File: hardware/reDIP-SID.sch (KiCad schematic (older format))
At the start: 57 parts, among them J1 Conn_01x04, J2 Conn_01x04, J3 Conn_01x10, J4 Conn_01x10, J5 TYPE-C-31-M-12, J6 Conn_02x05_Odd_Even, Q1 PDTA143ZMB, SW1 KXT331LHS, U1 NCP163AMX120TBG, U2 NCP167AMX330TBG, U3 SN74CBTD16211DGVR, U4 SGTL5000XNLA3, U5 NUF2042XV6, U6 APS6404L-3SQR-SN, U7 W25Q128JVPIM, U8 ICE40UP5K-SG48I, X1 ASCO-24.576MHZ-EK-T

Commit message: Usability and manufacturability improvements
* Made all iCE40 RGB pins externally available
* Removed split in stencil apertures for pin-in-paste
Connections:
- net labels added: USB_~CONN~
- net labels removed: USB_CONN
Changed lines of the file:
@@
 Text Label 1000 5900 2    50   ~ 0
 USB_D+
+Text Label 1000 7400 2    50   ~ 0
+ICE_~IO1~
 Text Label 1000 7100 2    50   ~ 0
-ICE_~IO1~
-Text Label 1000 7400 2    50   ~ 0
-USB_CONN
+USB_~CONN~
 $Comp
 L power:GND #PWR046
@@
 $EndComp
 Text Label 1800 2250 2    50   ~ 0
-USB_CONN
+USB_~CONN~
 Wire Wire Line
 	2200 2900 2200 3150
-Text Label 2200 2500 0    50   ~ 0
+Text Label 2200 2500 2    50   ~ 0
 USB_LINK
 Text Label 1950 3350 2    50   ~ 0

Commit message: Various fixes
* Added 10k pullup for SPI SCLK, following iCE40 Hardware Checklist
* Reworked USB routing to not rely on any particular ESD IC (note swapped pins)
* Widened a few tracks
* Added silk screen on back side for SPI header
* Increased courtyard for TVSOP-56 footprint
* Changed VCC to power symbol
* Corrected BOM for LDOs
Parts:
- added R12, R13: 0, Resistor_SMD:R_0201_0603Metric, symbol Device:R_Small
- added R7: 10k, Resistor_SMD:R_0201_0603Metric, symbol Device:R
- J6: Description CONN HEADER 2x5 POS .100\" SGL GOLD MATING 5.84mm TAIL 3.05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 -> CONN HEADER 2x5 POS .100\" DBL GOLD MATING 5.84mm TAIL 3.05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
- U1: PN NCP163AFCT120T2G -> NCP163AMX120TBG
- U2: PN NCP167AFCT330T2G -> NCP167AMX330TBG
- U4: Notes (none) -> ALTERNATIVE PART #: SGTL5000XNLA3R2; PN SGTL5000XNLA3R2 -> SGTL5000XNLA3
- U7: Notes (none) -> ALTERNATIVE PART #: W25Q128JVPIM TR
- renumbered R9 to R10, R10 to R11, R11 to R14, R7 to R8, R8 to R9
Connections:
- net labels added: VCC
- net labels removed: Vcc
- wire segments 355 -> 364
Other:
- moved on the sheet: Q1, R3

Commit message: Replaced non-stocked parts
* Replaced 1.2V LDO with more readily available part
* Changed oscillator reeling order number
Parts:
- U1: value NCP163AMX120TBG -> NCP115AMX120TCG; footprint ONSemi:CASE711AJ_1.0x1.0mm_P0.65mm -> ONSemi:CASE_711AJ_1.0x1.0mm_P0.65mm; symbol ONSemi:NCP163AMX120TBG -> ONSemi:NCP115AMX120TCG; Description IC REG LDO 1.2V 250mA XDFN4 -> IC REG LDO 1.2V 300mA XDFN4; PN NCP163AMX120TBG -> NCP115AMX120TCG
- U2: footprint ONSemi:CASE711AJ_1.0x1.0mm_P0.65mm -> ONSemi:CASE_711AJ_1.0x1.0mm_P0.65mm
- U5: footprint ONSemi:CASE463A_1.6x1.2mm_P0.5mm -> ONSemi:CASE_463A_1.6x1.2mm_P0.5mm
- X1: value ASCO-24.576MHZ-EK-T -> ASCO-24.576MHZ-EK-T3; PN ASCO-24.576MHZ-EK-T -> ASCO-24.576MHZ-EK-T3
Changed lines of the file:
@@
 Sheet 1 1
 Title "reDIP SID"
-Date "2021-03-03"
+Date "2021-04-18"
 Rev "0.1"
 Comp "Nimrod"
@@
 P 6150 7150
 F 0 "X1" H 6300 7400 50  0000 L CNN
-F 1 "ASCO-24.576MHZ-EK-T" H 5750 6850 50  0000 L CNN
+F 1 "ASCO-24.576MHZ-EK-T3" H 5750 6850 50  0000 L CNN
 F 2 "Oscillator:Oscillator_SMD_Abracon_ASCO-4Pin_1.6x1.2mm" H 6250 6800 50  0001 C CNN
 F 3 "https://abracon.com/Oscillators/ASCO.pdf" H 5925 7275 50  0001 C CNN
 F 4 "OSC 24.576 MHz" H 6150 7150 50  0001 C CNN "Description"
 F 5 "Abracon" H 6150 7150 50  0001 C CNN "Mfg"
-F 6 "ASCO-24.576MHZ-EK-T" H 6150 7150 50  0001 C CNN "PN"
+F 6 "ASCO-24.576MHZ-EK-T3" H 6150 7150 50  0001 C CNN "PN"
 	1    6150 7150
 	1    0    0    -1
@@
 F 0 "U2" H 5150 1465 50  0000 C CNN
 F 1 "NCP167AMX330TBG" H 5150 1374 50  0000 C CNN
-F 2 "ONSemi:CASE711AJ_1.0x1.0mm_P0.65mm" H 5150 1100 50  0001 C CNN
+F 2 "ONSemi:CASE_711AJ_1.0x1.0mm_P0.65mm" H 5150 1100 50  0001 C CNN
 F 3 "https://www.onsemi.com/pub/Collateral/NCP167-D.PDF" H 5150 1100 50  0001 C CNN
 F 4 "ON Semiconductor" H 5150 1100 50  0001 C CNN "Mfg"
@@
 $EndComp
 $Comp
-L ONSemi:NCP163AMX120TBG U1
+L ONSemi:NCP115AMX120TCG U1
 U 1 1 610BA994
 P 3550 1100
 F 0 "U1" H 3550 1465 50  0000 C CNN
-F 1 "NCP163AMX120TBG" H 3550 1374 50  0000 C CNN
-F 2 "ONSemi:CASE711AJ_1.0x1.0mm_P0.65mm" H 3550 1100 50  0001 C CNN
-F 3 "https://www.onsemi.com/pub/Collateral/NCP163-D.PDF" H 3550 1100 50  0001 C CNN
+F 1 "NCP115AMX120TCG" H 3550 1374 50  0000 C CNN
+F 2 "ONSemi:CASE_711AJ_1.0x1.0mm_P0.65mm" H 3550 1100 50  0001 C CNN
+F 3 "https://www.onsemi.com/pdf/datasheet/ncp115-d.pdf" H 3550 1100 50  0001 C CNN
 F 4 "ON Semiconductor" H 3550 1100 50  0001 C CNN "Mfg"
-F 5 "NCP163AMX120TBG" H 3550 1100 50  0001 C CNN "PN"
-F 6 "IC REG LDO 1.2V 250mA XDFN4" H 3550 1100 50  0001 C CNN "Description"
+F 5 "NCP115AMX120TCG" H 3550 1100 50  0001 C CNN "PN"
+F 6 "IC REG LDO 1.2V 300mA XDFN4" H 3550 1100 50  0001 C CNN "Description"
 	1    3550 1100
 	1    0    0    -1
@@
 F 0 "U5" H 2850 3650 50  0000 C CNN
 F 1 "NUF2042XV6" H 2600 2800 50  0000 C CNN
-F 2 "ONSemi:CASE463A_1.6x1.2mm_P0.5mm" H 2600 2750 50  0001 C CNN
+F 2 "ONSemi:CASE_463A_1.6x1.2mm_P0.5mm" H 2600 2750 50  0001 C CNN
 F 3 "https://www.onsemi.com/pub/Collateral/NUF2030XV6-D.PDF" H 2800 3600 50  0001 C CNN
 F 4 "IC USB TERMINATOR ESD PROTECTION SOT-563" H 2600 3250 50  0001 C CNN "Description"

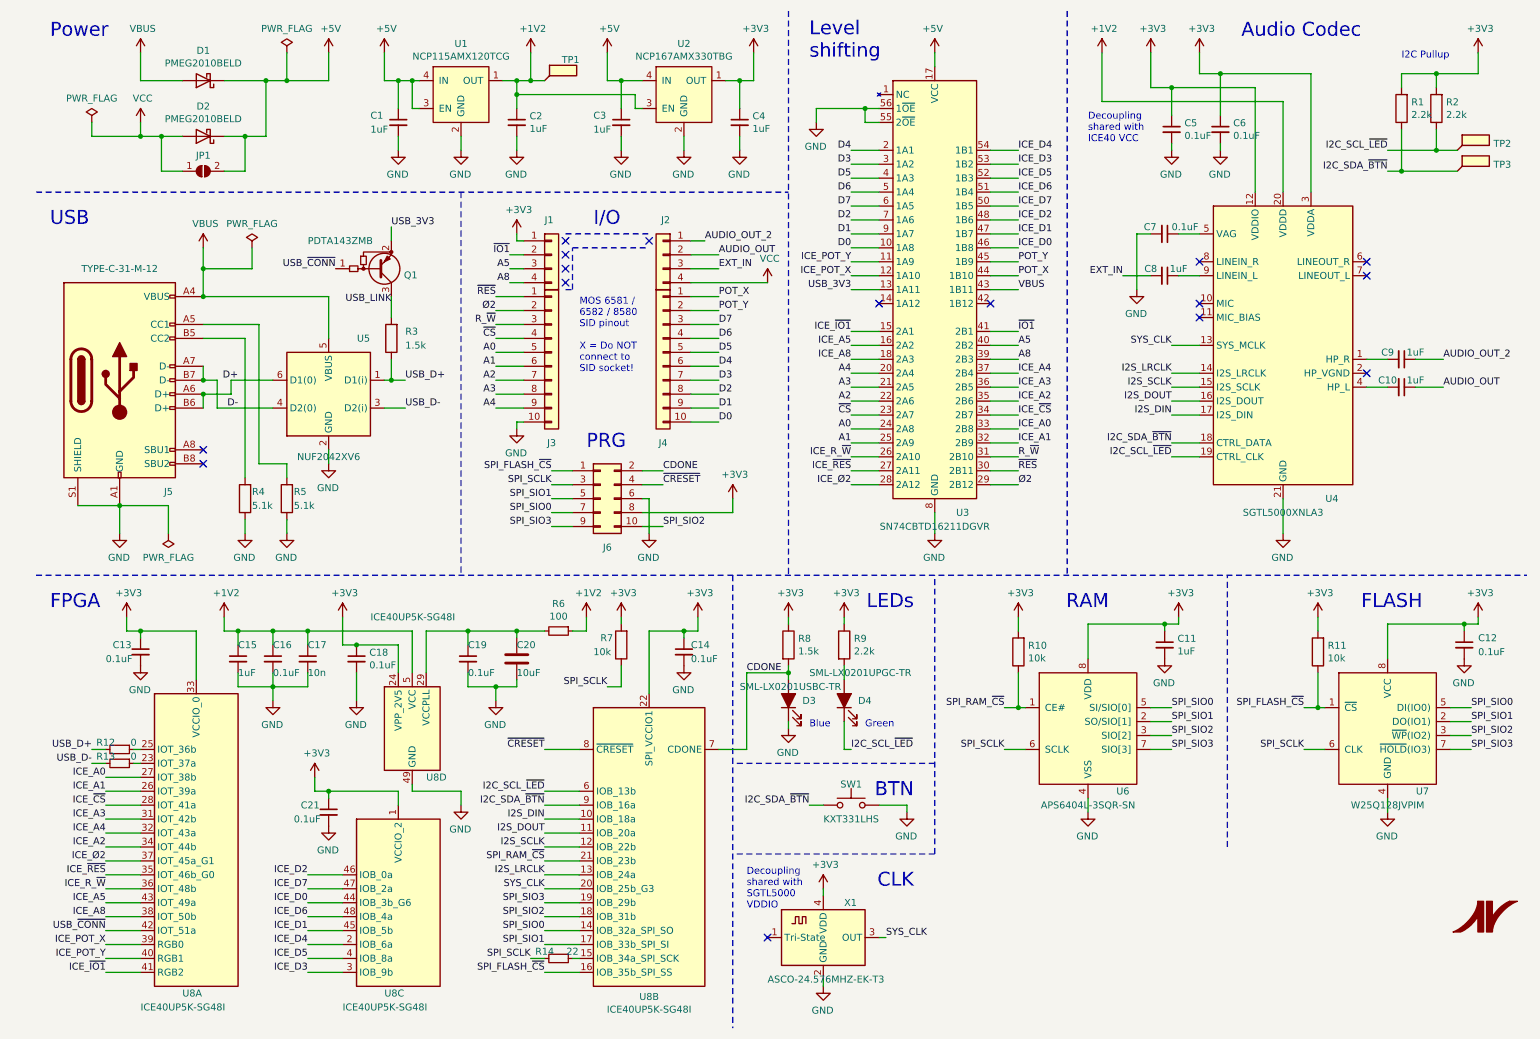
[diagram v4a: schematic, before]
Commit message: Showstopper fixes
* Pins swaps and rerouting to handle the fact that iCE40UP5K pins 35 and 37
  are output only when the PLL is used
* Removed Q1, USB_CONN is now used to pull up USB D+ directly through R3
* Changed the oscillator to 24 MHz (full speed USB is clocked at 12 MHz)
* Slight rounding of footprint pads for oscillator and button

Many thanks go to @smunaut for pointing out the (undocumented!) iCE40 PLL
peculiarities, and to zyp for pointing out that the PLL can't convert a
24.576MHz clock to anything that will work for full speed USB.
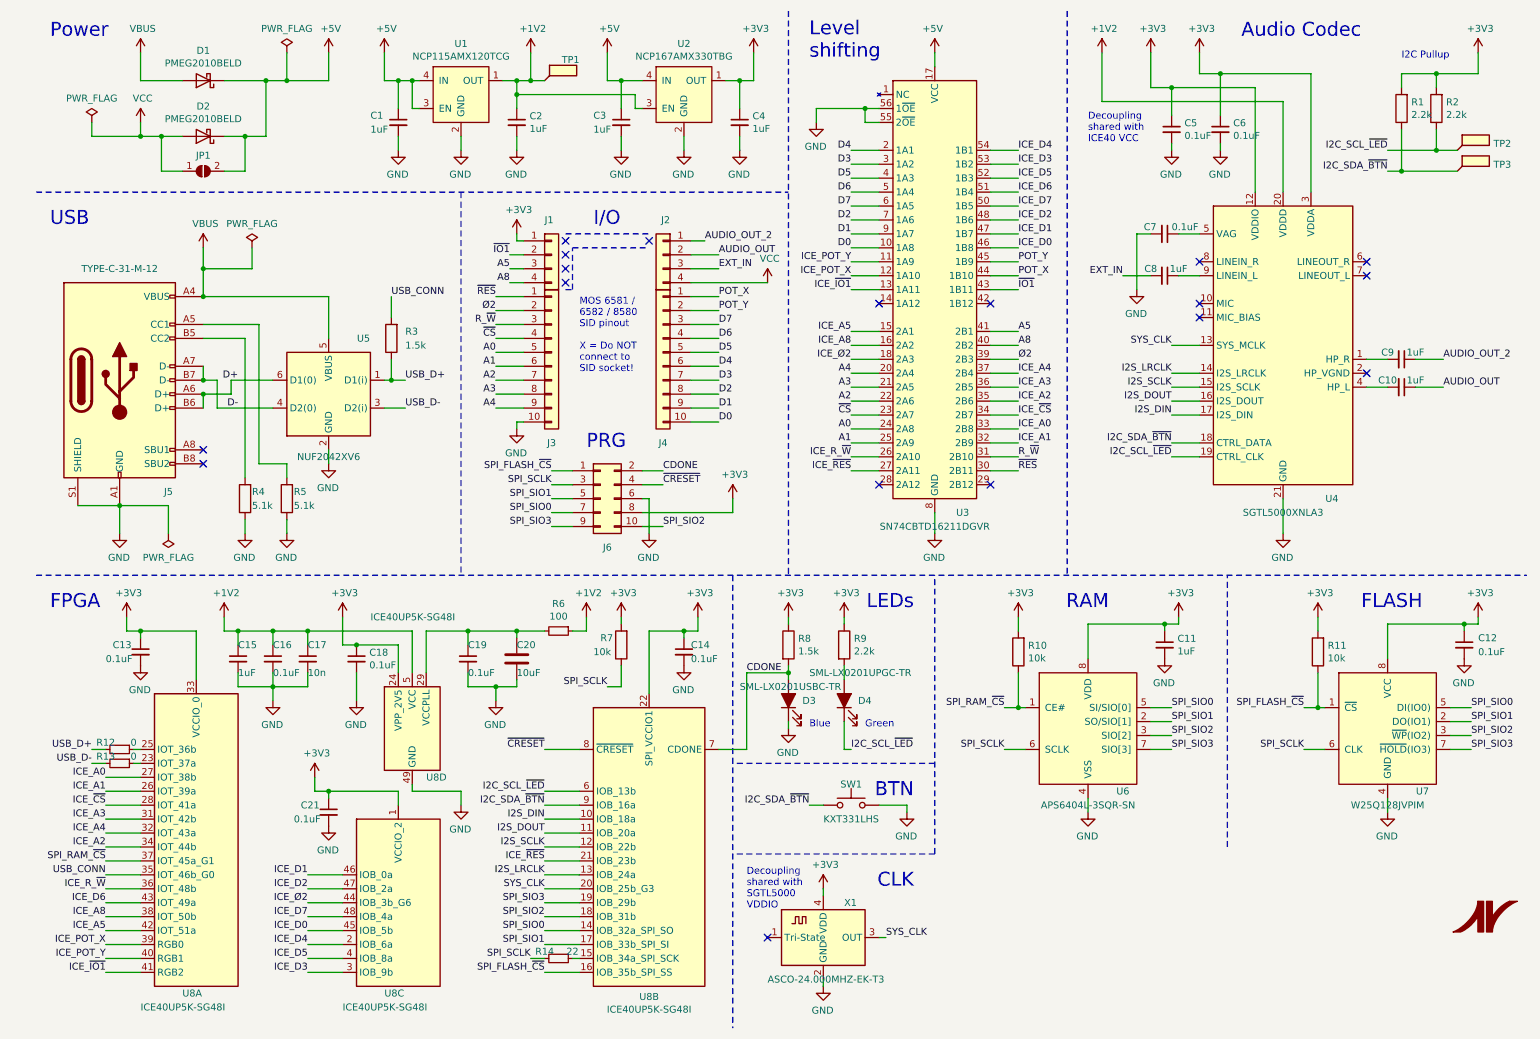
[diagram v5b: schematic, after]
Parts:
- removed Q1: PDTA143ZMB, Nexperia:SOT-883, symbol Device:Q_PNP_BEC_BRT
- SW1: footprint Button_Switch_SMD:SW_SPST_CK_KXT3 -> CK:SW_SPST_CK_KXT3
- X1: value ASCO-24.576MHZ-EK-T3 -> ASCO-24.000MHZ-EK-T3; footprint Oscillator:Oscillator_SMD_Abracon_ASCO-4Pin_1.6x1.2mm -> reDIP:Oscillator_SMD-4Pin_1.6x1.2mm; Description OSC 24.576 MHz -> OSC 24 MHz 30 ppm 1.6x1.2 mm; PN ASCO-24.576MHZ-EK-T3 -> ASCO-24.000MHZ-EK-T3
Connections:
- net USB_3V3 is gone; now on net ICE_~IO1~: U3.13 (1A11)
- net USB_~CONN~ is gone; now on net ICE_A5: U8.42 (IOT_51a)
- net A5: now also U3.41 (2B1); no longer U3.40 (2B2)
- net A8: now also U3.40 (2B2); no longer U3.39 (2B3)
- net ICE_A5: now also U3.15 (2A1); no longer U3.16 (2A2), U8.43 (IOT_49a)
- net ICE_A8: now also U3.16 (2A2); no longer U3.18 (2A3)
- net ICE_D0: now also U8.45 (IOB_5b); no longer U8.44 (IOB_3b_G6)
- net ICE_D1: now also U8.46 (IOB_0a); no longer U8.45 (IOB_5b)
- net ICE_D2: now also U8.47 (IOB_2a); no longer U8.46 (IOB_0a)
- net ICE_D6: now also U8.43 (IOT_49a); no longer U8.48 (IOB_4a)
- net ICE_D7: now also U8.48 (IOB_4a); no longer U8.47 (IOB_2a)
- net ICE_~IO1~: no longer U3.15 (2A1)
- net ICE_~RES~: now also U8.21 (IOB_23b); no longer U8.35 (IOT_46b_G0)
- net ICE_Ø2: now also U3.18 (2A3), U8.44 (IOB_3b_G6); no longer U3.28 (2A12), U8.37 (IOT_45a_G1)
- net SPI_RAM_~CS~: now also U8.37 (IOT_45a_G1); no longer U8.21 (IOB_23b)
- net VBUS: no longer U3.43 (1B11)
- net ~IO1~: now also U3.43 (1B11); no longer U3.41 (2B1)
- net Ø2: now also U3.39 (2B3); no longer U3.29 (2B12)
- net USB_LINK renamed USB_CONN
- net USB_CONN: now also U8.35 (IOT_46b_G0)
- no-connect marks 16 -> 18
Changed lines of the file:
@@
 Sheet 1 1
 Title "reDIP SID"
-Date "2021-04-21"
+Date "2021-04-25"
 Rev "0.2"
 Comp "Nimrod"
@@
 P 6150 7150
 F 0 "X1" H 6300 7400 50  0000 L CNN
-F 1 "ASCO-24.576MHZ-EK-T3" H 5750 6850 50  0000 L CNN
-F 2 "Oscillator:Oscillator_SMD_Abracon_ASCO-4Pin_1.6x1.2mm" H 6250 6800 50  0001 C CNN
+F 1 "ASCO-24.000MHZ-EK-T3" H 5750 6850 50  0000 L CNN
+F 2 "reDIP:Oscillator_SMD-4Pin_1.6x1.2mm" H 6250 6800 50  0001 C CNN
 F 3 "https://abracon.com/Oscillators/ASCO.pdf" H 5925 7275 50  0001 C CNN
-F 4 "OSC 24.576 MHz" H 6150 7150 50  0001 C CNN "Description"
+F 4 "OSC 24 MHz 30 ppm 1.6x1.2 mm" H 6150 7150 50  0001 C CNN "Description"
 F 5 "Abracon" H 6150 7150 50  0001 C CNN "Mfg"
-F 6 "ASCO-24.576MHZ-EK-T3" H 6150 7150 50  0001 C CNN "PN"
+F 6 "ASCO-24.000MHZ-EK-T3" H 6150 7150 50  0001 C CNN "PN"
 	1    6150 7150
 	1    0    0    -1
@@
 Text Label 7550 2400 0    50   ~ 0
 POT_X
-Text Label 7550 3000 0    50   ~ 0
+Text Label 7550 2900 0    50   ~ 0
 A8
-Text Label 7550 2900 0    50   ~ 0
+Text Label 7550 2800 0    50   ~ 0
 A5
 $Comp
@@
 	1    0    0    -1
 $EndComp
-Text Label 7550 2500 0    50   ~ 0
-VBUS
 Wire Wire Line
 	7350 3000 7550 3000
-Text Label 6350 2500 2    50   ~ 0
-USB_3V3
 Wire Wire Line
 	6550 3000 6350 3000
@@
 Text Label 7550 1900 0    50   ~ 0
 ICE_D7
-Wire Wire Line
-	6550 3900 6350 3900
 Text Label 6350 3700 2    50   ~ 0
 ICE_R_~W~
+Text Label 6350 2800 2    50   ~ 0
+ICE_A5
 Text Label 6350 2900 2    50   ~ 0
-ICE_A5
-Text Label 6350 3000 2    50   ~ 0
 ICE_A8
-Text Label 6350 2800 2    50   ~ 0
+Text Label 6350 2500 2    50   ~ 0
 ICE_~IO1~
-Text Label 7550 2800 0    50   ~ 0
+Text Label 7550 2500 0    50   ~ 0
 ~IO1~
 Wire Wire Line
@@
 Wire Wire Line
 	6550 3500 6350 3500
-Wire Wire Line
-	7350 3900 7550 3900
 Text Label 6350 3100 2    50   ~ 0
 A4
@@
 Text Label 7550 3700 0    50   ~ 0
 R_~W~
-Text Label 7550 3900 0    50   ~ 0
+Text Label 7550 3000 0    50   ~ 0
 Ø2
 Wire Wire Line
@@
 Text Label 6350 3800 2    50   ~ 0
 ICE_~RES~
-Text Label 6350 3900 2    50   ~ 0
+Text Label 6350 3000 2    50   ~ 0
 ICE_Ø2
 Text Label 7550 3400 0    50   ~ 0
@@
 Wire Wire Line
 	2500 6100 2600 6100
-Text Label 2450 6700 2    50   ~ 0
-ICE_D2
-Text Label 2450 7200 2    50   ~ 0
-ICE_D4
-Text Label 2450 7300 2    50   ~ 0
-ICE_D5
 Wire Wire Line
 	2450 7400 2700 7400
 Wire Wire Line
 	2450 7300 2700 7300
-Text Label 2450 6800 2    50   ~ 0
-ICE_D7
-Text Label 2450 7000 2    50   ~ 0
-ICE_D6
-Text Label 2450 6900 2    50   ~ 0
-ICE_D0
-Text Label 2450 7400 2    50   ~ 0
-ICE_D3
-Text Label 2450 7100 2    50   ~ 0
-ICE_D1
 Wire Wire Line
 	2450 7000 2700 7000
@@
 Text Label 1000 6000 2    50   ~ 0
 ICE_A0
-Text Label 1000 6700 2    50   ~ 0
+Text Label 4150 6600 2    50   ~ 0
 ICE_~RES~
-Text Label 1000 6600 2    50   ~ 0
+Text Label 2450 6900 2    50   ~ 0
 ICE_Ø2
 Wire Wire Line
@@
 Wire Wire Line
 	1200 5800 1250 5800
-Text Label 1000 6900 2    50   ~ 0
+Text Label 1000 7100 2    50   ~ 0
 ICE_A5
 Text Label 1000 7000 2    50   ~ 0
@@
 Text Label 1000 7400 2    50   ~ 0
 ICE_~IO1~
-Text Label 1000 7100 2    50   ~ 0
-USB_~CONN~
 $Comp
 L power:GND #PWR049
@@
 Text Label 4150 6400 2    50   ~ 0
 I2S_DOUT
-Text Label 4150 6600 2    50   ~ 0
+Text Label 1000 6600 2    50   ~ 0
 SPI_RAM_~CS~
 Wire Wire Line
@@
 F 0 "SW1" H 6350 6350 50  0000 C CNN
 F 1 "KXT331LHS" H 6350 6100 50  0000 C CNN
-F 2 "Button_Switch_SMD:SW_SPST_CK_KXT3" H 6350 6400 50  0001 C CNN
+F 2 "CK:SW_SPST_CK_KXT3" H 6350 6400 50  0001 C CNN
 F 3 "https://www.ckswitches.com/media/1465/kxt3.pdf" H 6350 6400 50  0001 C CNN
 F 4 "SW TACT 3.0 x 2.0 mm" H 6350 6200 50  0001 C CNN "Description"
@@
 Text Label 3150 3150 0    50   ~ 0
 USB_D+
-Wire Wire Line
-	3050 2150 3050 2050
-Text Label 3050 2600 2    50   ~ 0
-USB_LINK
-Text Label 2650 2350 2    50   ~ 0
-USB_~CONN~
-$Comp
-L Device:Q_PNP_BEC_BRT Q1
-U 1 1 61E05EF8
-P 3000 2350
-F 0 "Q1" H 3140 2396 50  0000 L CNN
-F 1 "PDTA143ZMB" H 2450 2150 50  0000 L CNN
-F 2 "Nexperia:SOT-883" H 3000 2350 50  0001 C CNN
-F 3 "https://assets.nexperia.com/documents/data-sheet/PDTA143ZMB.pdf" H 3000 2350 50  0001 C CNN
-F 4 "TRANSISTOR PNP RET R1=4.7kΩ R2=47kΩ 100mA SOT883B" H 3000 2350 50  0001 C CNN "Description"
-F 5 "Nexperia" H 3000 2350 50  0001 C CNN "Mfg"
-F 6 "PDTA143ZMB\\,315" H 3000 2350 50  0001 C CNN "PN"
-	1    3000 2350
-	1    0    0    1
-$EndComp
-Text Label 3050 2050 0    50   ~ 0
-USB_3V3
+Text Label 3050 2550 0    50   ~ 0
+USB_CONN
 Wire Wire Line
 	3050 3000 3050 3150
@@
 Wire Wire Line
 	3050 2700 3050 2550
+Text Label 1000 6700 2    50   ~ 0
+USB_CONN
+Text Label 2450 7000 2    50   ~ 0
+ICE_D7
+Text Label 2450 7300 2    50   ~ 0
+ICE_D5
+Text Label 2450 7200 2    50   ~ 0
+ICE_D4
+Text Label 2450 7400 2    50   ~ 0
+ICE_D3
+Text Label 2450 6800 2    50   ~ 0
+ICE_D2
+Text Label 2450 6700 2    50   ~ 0
+ICE_D1
+Text Label 1000 6900 2    50   ~ 0
+ICE_D6
+Text Label 2450 7100 2    50   ~ 0
+ICE_D0
+NoConn ~ 6550 3900
+NoConn ~ 7350 3900
 $EndSCHEMATC

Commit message: Preparing for prototyping
* Routing cleanups
* Changed oscillator to ± 25 ppm part
* Note on the PLL output-only-pin trap in the schematic

Thanks to @DX-MON for pointing out that audio hardware should have
as high frequency stability as possible.
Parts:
- X1: value ASCO-24.000MHZ-EK-T3 -> ECS-1612MV-240-CN-TR; symbol Oscillator:ASCO -> ECS:ECS-1612MV-240-CN-TR; Description OSC 24 MHz 30 ppm 1.6x1.2 mm -> OSC 24 MHz 25 ppm 1.6x1.2 mm; Mfg Abracon -> ECS; PN ASCO-24.000MHZ-EK-T3 -> ECS-1612MV-240-CN-TR
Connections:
- net +3V3: now also X1.1 (Tri-State)
- net ICE_R_~W~: now also U3.27 (2A11); no longer U3.26 (2A10)
- net ICE_~RES~: now also U3.28 (2A12); no longer U3.27 (2A11)
- net R_~W~: now also U3.30 (2B11); no longer U3.31 (2B10)
- net ~RES~: now also U3.29 (2B12); no longer U3.30 (2B11)
- no-connect marks 18 -> 17
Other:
- note added: "Note: G0 and G1\nbecome output-only\nwhen the PLL is used"
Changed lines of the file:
@@
 NoConn ~ 8850 2300
 $Comp
-L Oscillator:ASCO X1
+L ECS:ECS-1612MV-240-CN-TR X1
 U 1 1 5FCDB7D7
 P 6150 7150
 F 0 "X1" H 6300 7400 50  0000 L CNN
-F 1 "ASCO-24.000MHZ-EK-T3" H 5750 6850 50  0000 L CNN
+F 1 "ECS-1612MV-240-CN-TR" H 5750 6850 50  0000 L CNN
 F 2 "reDIP:Oscillator_SMD-4Pin_1.6x1.2mm" H 6250 6800 50  0001 C CNN
-F 3 "https://abracon.com/Oscillators/ASCO.pdf" H 5925 7275 50  0001 C CNN
-F 4 "OSC 24 MHz 30 ppm 1.6x1.2 mm" H 6150 7150 50  0001 C CNN "Description"
-F 5 "Abracon" H 6150 7150 50  0001 C CNN "Mfg"
-F 6 "ASCO-24.000MHZ-EK-T3" H 6150 7150 50  0001 C CNN "PN"
+F 3 "https://ecsxtal.com/store/pdf/ECS-1612MV.pdf" H 5925 7275 50  0001 C CNN
+F 4 "OSC 24 MHz 25 ppm 1.6x1.2 mm" H 6150 7150 50  0001 C CNN "Description"
+F 5 "ECS" H 6150 7150 50  0001 C CNN "Mfg"
+F 6 "ECS-1612MV-240-CN-TR" H 6150 7150 50  0001 C CNN "PN"
 	1    6150 7150
 	1    0    0    -1
@@
 	1    0    0    -1
 $EndComp
-NoConn ~ 5750 7150
 Wire Wire Line
 	6550 7150 6600 7150
@@
 Text Label 10600 3000 0    50   ~ 0
 AUDIO_OUT_2
-Text Notes 5600 6950 0    50   ~ 0
+Text Notes 5550 6900 0    50   ~ 0
 Decoupling\nshared with\nSGTL5000\nVDDIO
 $Comp
@@
 Text Label 7550 1900 0    50   ~ 0
 ICE_D7
-Text Label 6350 3700 2    50   ~ 0
+Text Label 6350 3800 2    50   ~ 0
 ICE_R_~W~
 Text Label 6350 2800 2    50   ~ 0
@@
 	7550 2500 7350 2500
 Wire Wire Line
-	7350 3800 7550 3800
-Wire Wire Line
-	6350 3800 6550 3800
-Text Label 7550 3800 0    50   ~ 0
+	7350 3900 7550 3900
+Wire Wire Line
+	6350 3900 6550 3900
+Text Label 7550 3900 0    50   ~ 0
 ~RES~
 Wire Wire Line
@@
 Text Label 6350 3500 2    50   ~ 0
 A0
-Text Label 7550 3700 0    50   ~ 0
+Text Label 7550 3800 0    50   ~ 0
 R_~W~
 Text Label 7550 3000 0    50   ~ 0
@@
 	7550 2800 7350 2800
 Wire Wire Line
-	7550 3700 7350 3700
+	7550 3800 7350 3800
 Wire Wire Line
 	7550 1600 7350 1600
@@
 	7350 2900 7550 2900
 Wire Wire Line
-	6350 3700 6550 3700
+	6350 3800 6550 3800
 Wire Wire Line
 	6350 2500 6550 2500
@@
 Text Label 6350 2400 2    50   ~ 0
 ICE_POT_X
-Text Label 6350 3800 2    50   ~ 0
+Text Label 6350 3900 2    50   ~ 0
 ICE_~RES~
 Text Label 6350 3000 2    50   ~ 0
@@
 Text Label 2450 7100 2    50   ~ 0
 ICE_D0
-NoConn ~ 6550 3900
-NoConn ~ 7350 3900
+NoConn ~ 6550 3700
+NoConn ~ 7350 3700
+Wire Wire Line
+	6150 6850 5750 6850
+Wire Wire Line
+	5750 6850 5750 7150
+Connection ~ 6150 6850
+Text Notes 500  5650 0    50   ~ 0
+Note: G0 and G1\nbecome output-only\nwhen the PLL is used
 $EndSCHEMATC
